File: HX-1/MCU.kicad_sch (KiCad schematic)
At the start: 37 parts, among them J10 Conn_01x22, J11 Conn_01x08, J12 USART_CONN, J3 I2C_CONN, J4 SPI_CONN, J7 FDCAN_CONN, J8 UART_CONN, J9 Conn_01x22, SW1 SW_SPDT, U1 STM32H723ZGT6

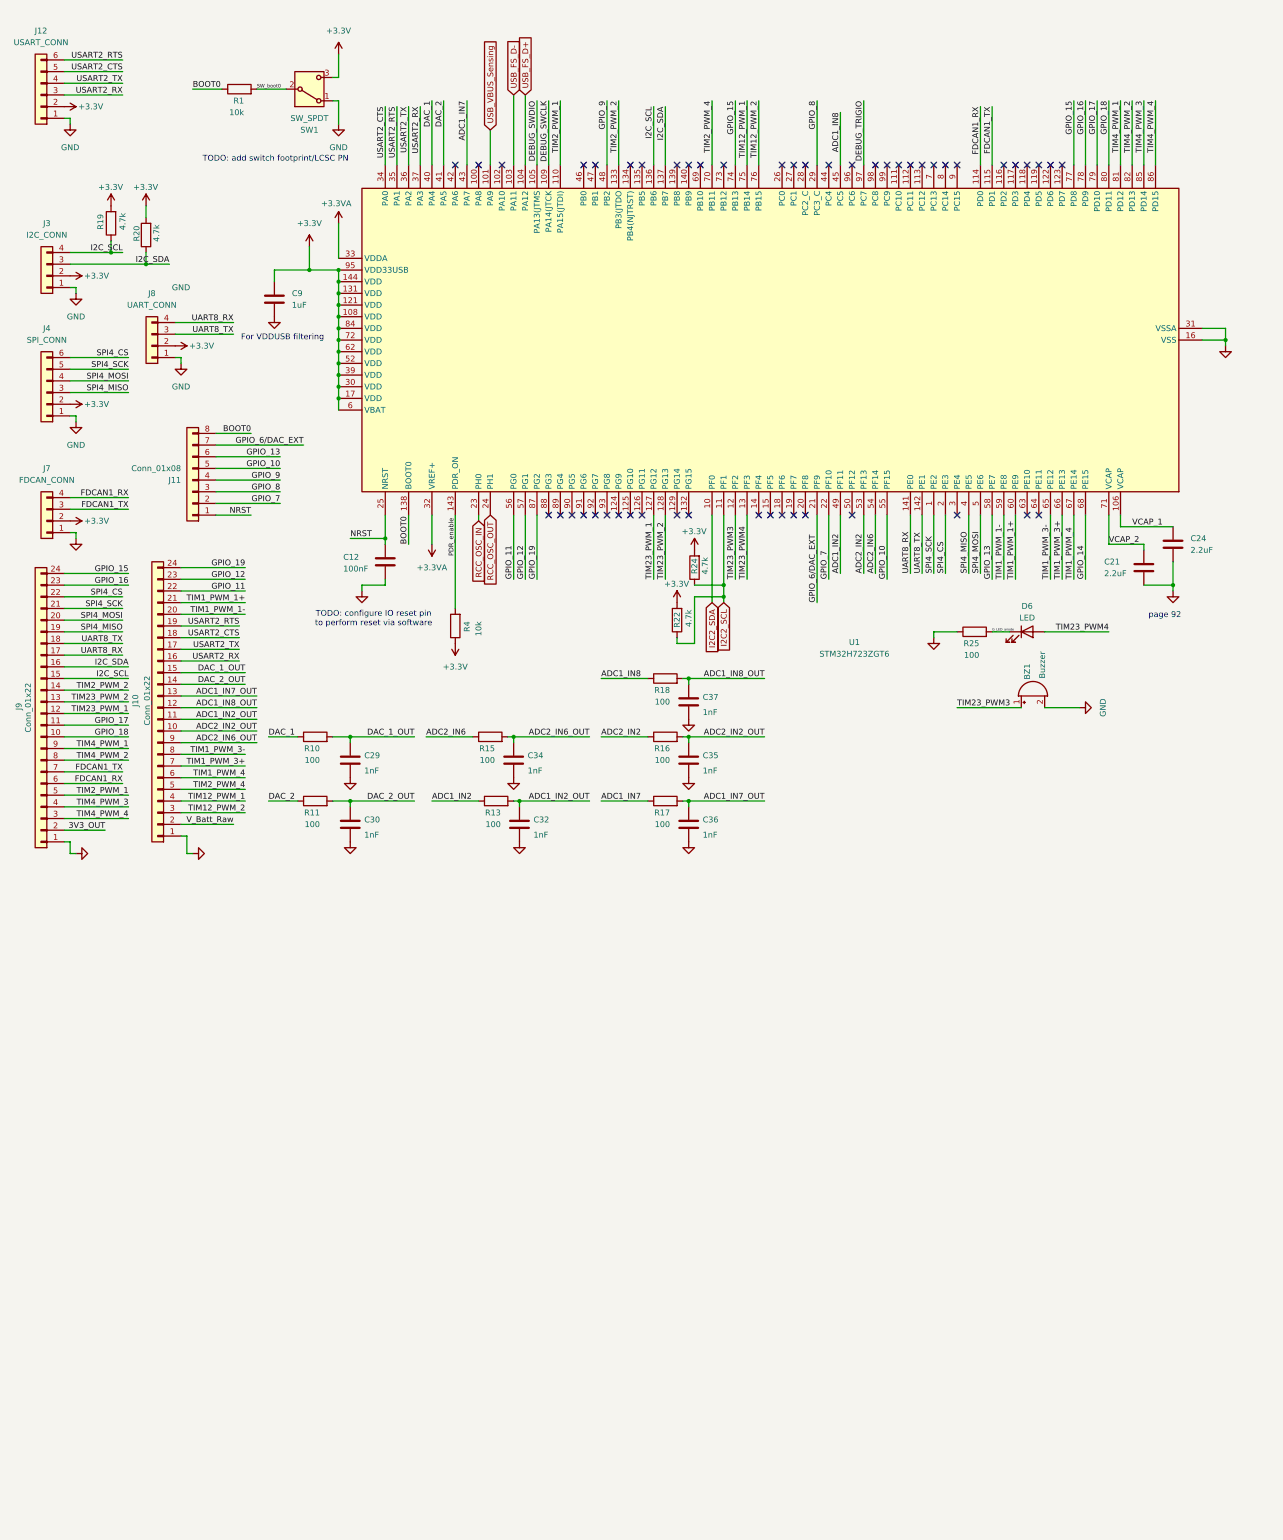
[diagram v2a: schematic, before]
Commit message: change GPIO locations to optimise for output headers
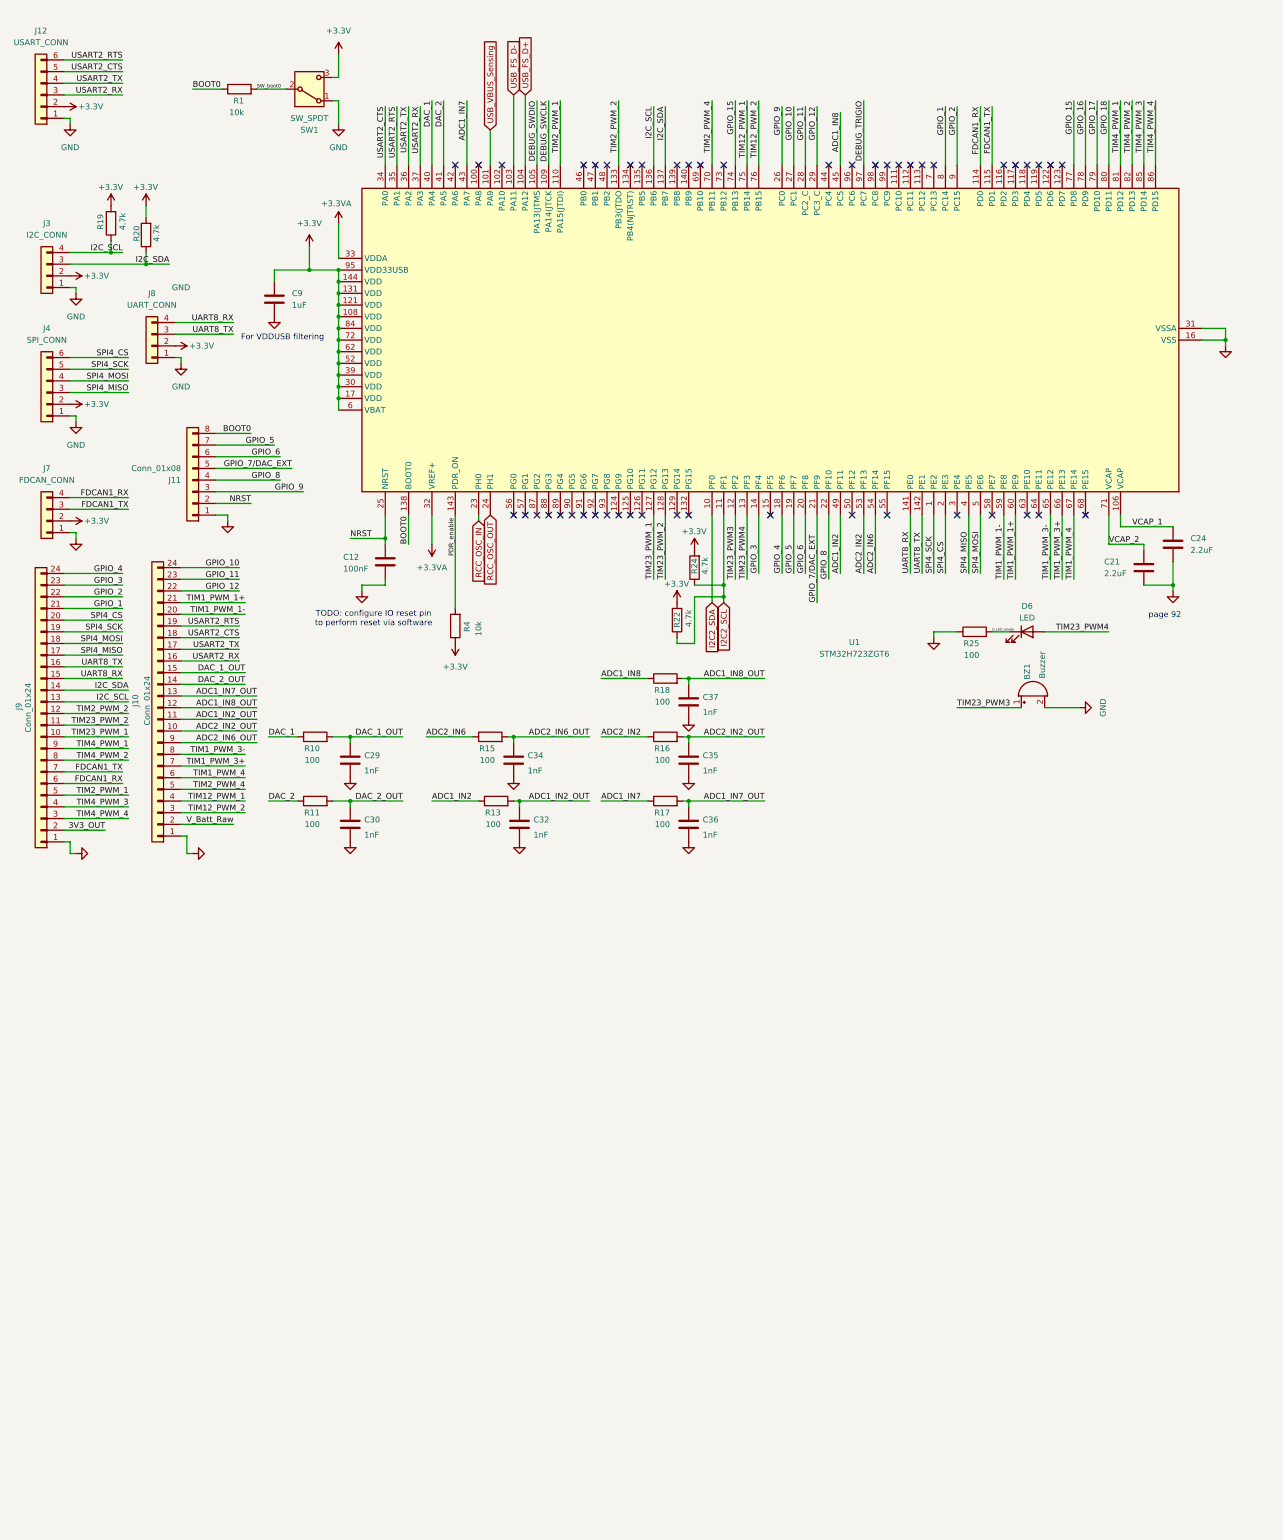
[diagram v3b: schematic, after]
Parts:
- J10, J9: value Conn_01x22 -> Conn_01x24
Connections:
- net GND: now also J11.1 (Pin_1)
- net GPIO_10: now also J10.24 (Pin_24), U1.27 (PC1); no longer J11.5 (Pin_5), U1.55 (PF15)
- net GPIO_11: now also J10.23 (Pin_23), U1.28 (PC2_C); no longer J10.22 (Pin_22), U1.56 (PG0)
- net GPIO_12: now also J10.22 (Pin_22), U1.29 (PC3_C); no longer J10.23 (Pin_23), U1.57 (PG1)
- net GPIO_15: no longer J9.24 (Pin_24)
- net GPIO_16: no longer J9.23 (Pin_23)
- net GPIO_17: no longer J9.11 (Pin_11)
- net GPIO_18: no longer J9.10 (Pin_10)
- net GPIO_8: now also J11.4 (Pin_4), U1.22 (PF10); no longer J11.3 (Pin_3), U1.29 (PC3_C)
- net GPIO_9: now also J11.3 (Pin_3), U1.26 (PC0); no longer J11.4 (Pin_4), U1.48 (PB2)
- net I2C_SCL: now also J9.13 (Pin_13); no longer J9.15 (Pin_15)
- net I2C_SDA: now also J9.14 (Pin_14); no longer J9.16 (Pin_16)
- net NRST: now also J11.2 (Pin_2); no longer J11.1 (Pin_1)
- net SPI4_CS: now also J9.20 (Pin_20); no longer J9.22 (Pin_22)
- net SPI4_MISO: now also J9.17 (Pin_17); no longer J9.19 (Pin_19)
- net SPI4_MOSI: now also J9.18 (Pin_18); no longer J9.20 (Pin_20)
- net SPI4_SCK: now also J9.19 (Pin_19); no longer J9.21 (Pin_21)
- net TIM23_PWM_1: now also J9.10 (Pin_10); no longer J9.12 (Pin_12)
- net TIM23_PWM_2: now also J9.11 (Pin_11); no longer J9.13 (Pin_13)
- net TIM2_PWM_2: now also J9.12 (Pin_12); no longer J9.14 (Pin_14)
- net UART8_RX: now also J9.15 (Pin_15); no longer J9.17 (Pin_17)
- net UART8_TX: now also J9.16 (Pin_16); no longer J9.18 (Pin_18)
- net GPIO_3: now reaches U1.14 (PF4)
- net GPIO_3: now also J9.23 (Pin_23)
- net GPIO_4: now reaches U1.18 (PF6)
- net GPIO_4: now also J9.24 (Pin_24)
- net GPIO_5: now reaches U1.19 (PF7)
- net GPIO_5: now also J11.7 (Pin_7)
- net GPIO_6: now reaches U1.20 (PF8)
- net GPIO_6: now also J11.6 (Pin_6)
- net GPIO_1: now reaches U1.8 (PC14)
- net GPIO_1: now also J9.21 (Pin_21)
- net GPIO_2: now reaches U1.9 (PC15)
- net GPIO_2: now also J9.22 (Pin_22)
- net GPIO_13: no longer names the net of U1.58 (PE7)
- net GPIO_13: no longer J11.6 (Pin_6)
- net GPIO_14: no longer names the net of U1.68 (PE15)
- net GPIO_19: no longer names the net of U1.87 (PG2)
- net GPIO_19: no longer J10.24 (Pin_24)
- net GPIO_6/DAC_EXT renamed GPIO_7/DAC_EXT
- net GPIO_7/DAC_EXT: now also J11.5 (Pin_5); no longer J11.7 (Pin_7)
- removed net GPIO_7: J11.2 (Pin_2), U1.22 (PF10)
- no-connect marks 50 -> 48
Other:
- note removed: "TODO: add switch footprint/LCSC PN"

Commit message: clean up schematic, layout more of pcb, fix some footprints
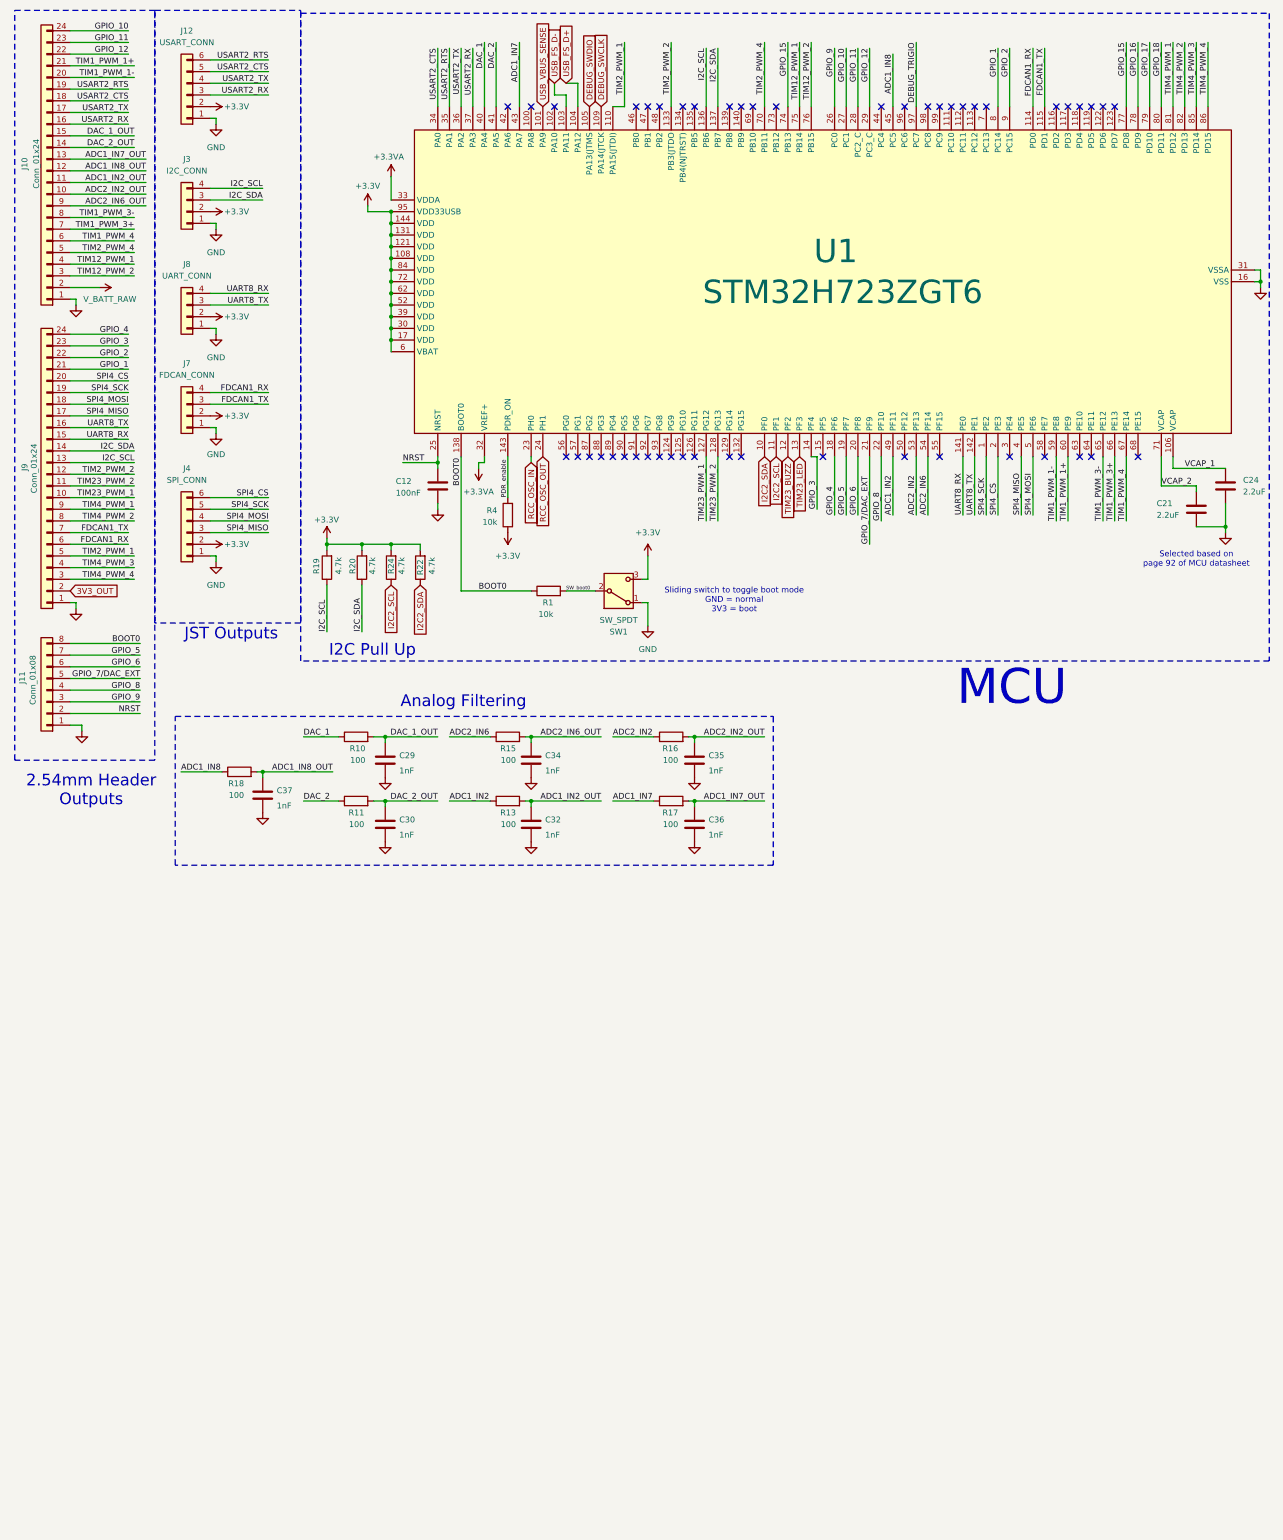
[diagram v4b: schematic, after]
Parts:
- removed BZ1: Buzzer, Buzzer:YUEXIN YX-SMD5020, symbol Device:Buzzer
- removed C9: 1uF, Capacitor_SMD:C_0603_1608Metric, symbol Device:C
- removed D6: LED, LED_SMD:LED_0805_2012Metric, symbol Device:LED
- removed R25: 100, Resistor_SMD:R_0402_1005Metric, symbol Device:R
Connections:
- net I2C2_SCL: no longer R22.1
- net I2C2_SDA: now also R22.1
- net TIM23_PWM3 renamed TIM23_BUZZ
- net TIM23_PWM4 renamed TIM23_LED
- net USB_VBUS_Sensing renamed USB_VBUS_SENSE
- net V_Batt_Raw renamed V_BATT_RAW
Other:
- note added: "2.54mm Header Outputs"
- note added: "Analog Filtering"
- note added: "I2C Pull Up"
- note added: "JST Outputs"
- note added: "MCU"
- note added: "Selected based on page 92 of MCU datasheet"
- note added: "Sliding switch to toggle boot mode GND = normal 3V3 = boot"
- note removed: "For VDDUSB filtering"
- note removed: "TODO: configure IO reset pin to perform reset via software"
- note removed: "page 92"
- moved on the sheet: C12, C21, C24, C29, C30, C32, C34, C35, C36, C37, J10, J11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
